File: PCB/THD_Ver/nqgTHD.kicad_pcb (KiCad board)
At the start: 2 copper layers, 215.5 x 81 mm, 85 parts, among them SW1 SW_PUSH, SW10 SW_PUSH, SW11 SW_PUSH, SW12 SW_PUSH, SW13 SW_PUSH, SW14 SW_PUSH, SW15 SW_PUSH, SW16 SW_PUSH, SW17 SW_PUSH, SW18 SW_PUSH, SW19 SW_PUSH, SW2 SW_PUSH, SW20 SW_PUSH, SW21 SW_PUSH, SW22 SW_PUSH, SW23 SW_PUSH, SW24 SW_PUSH, SW25 SW_PUSH, SW26 SW_PUSH, SW27 SW_PUSH, SW28 SW_PUSH, SW29 SW_PUSH, SW3 SW_PUSH, SW30 SW_PUSH, SW31 SW_PUSH, SW32 SW_PUSH, SW33 SW_PUSH, SW34 SW_PUSH, SW35 SW_PUSH, SW36 SW_PUSH, SW37 SW_PUSH, SW38 SW_PUSH, SW39 SW_PUSH, SW4 SW_PUSH, SW40 SW_PUSH, SW5 SW_PUSH, SW6 SW_PUSH, SW7 SW_PUSH, SW8 SW_PUSH, SW9 SW_PUSH, U1 ProMicro

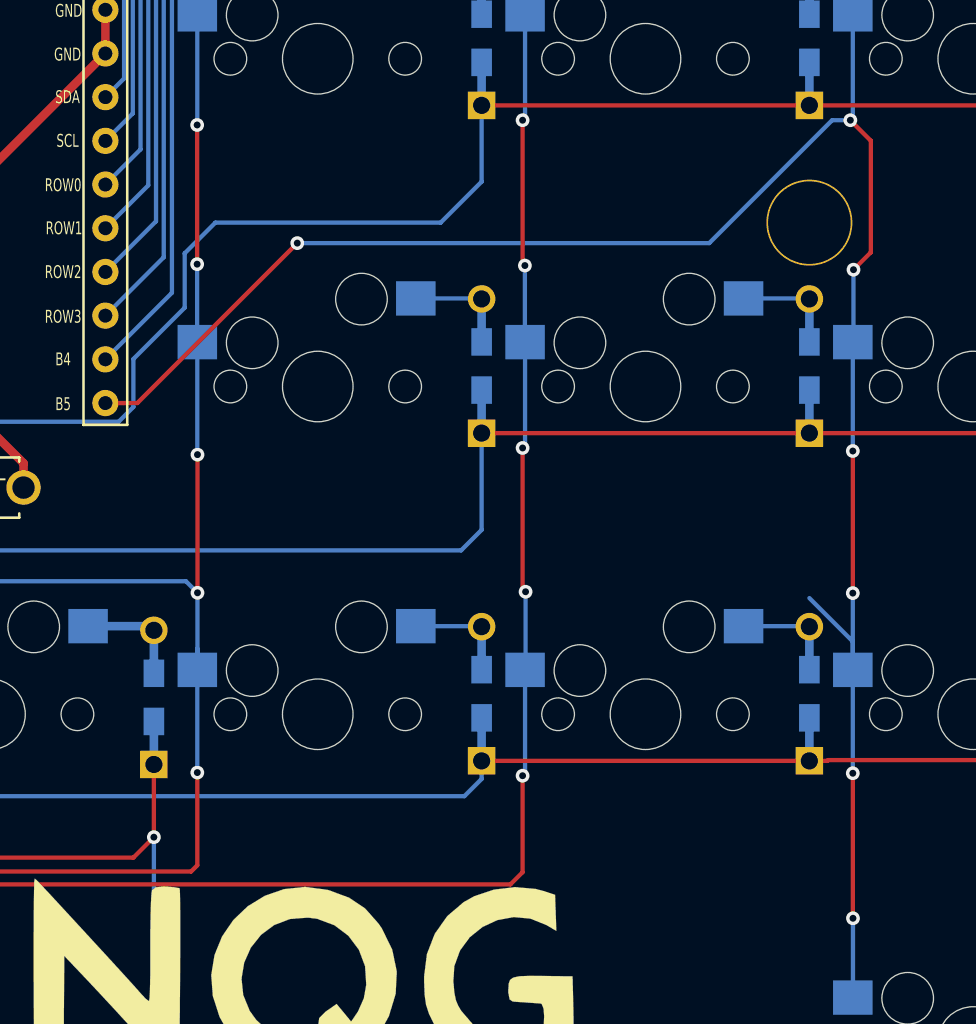
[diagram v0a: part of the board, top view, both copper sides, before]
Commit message: added new screw to THD version, created new plates with new screw locations
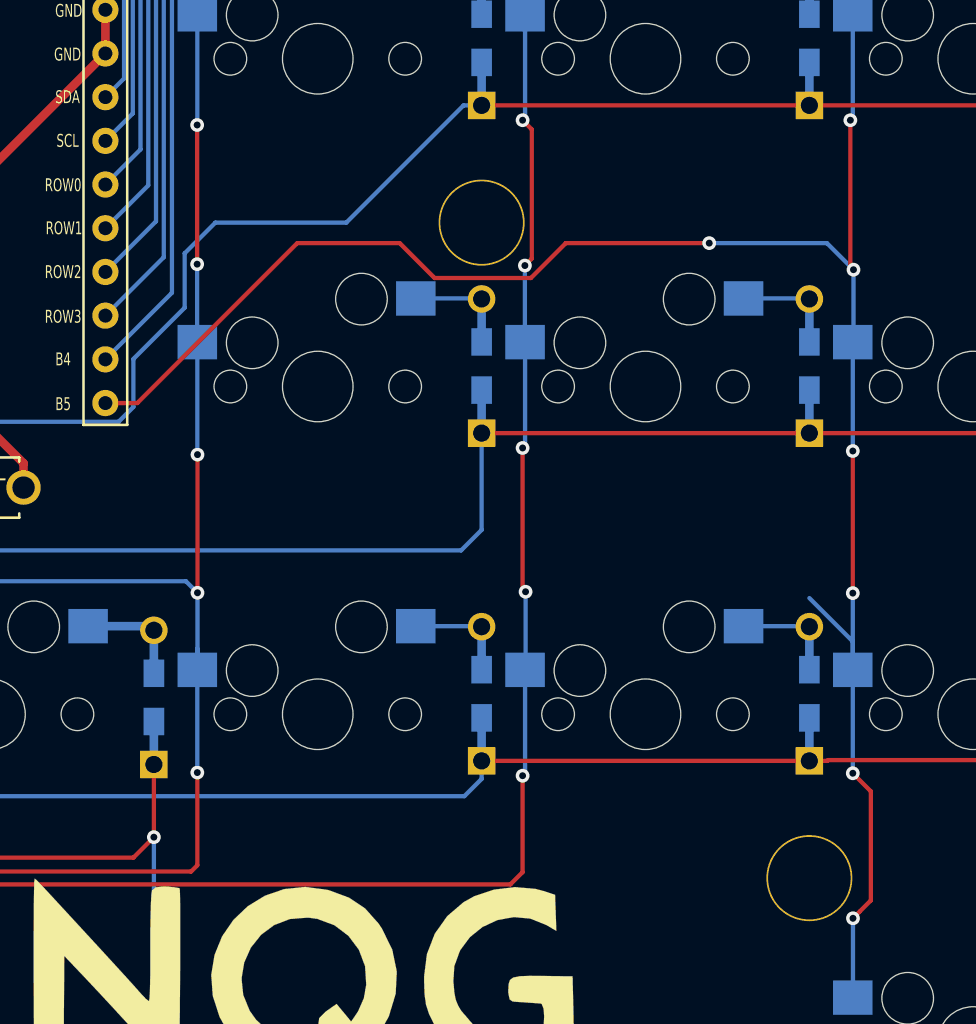
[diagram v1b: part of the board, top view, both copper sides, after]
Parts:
- removed the Ref** at (200.0, 142.9)
- added Ref**: Val**, kbd:HOLE, F.Cu at (200.0, 181.0)
- added Ref**: Val**, kbd:HOLE, F.Cu at (181.0, 142.9)
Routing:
- net row0: track 223.2 -> 220.6 mm
- net col1: track 134.2 -> 134.7 mm
